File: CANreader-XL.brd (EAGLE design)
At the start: 61 x 66.5 mm, 77 parts, among them IC2 TJA1055T, IC3 BD9G101G, IC4 LM1117IMPX-3.3, IC5 STM32F107VBT, Q1 16MHz, SW1 SLEEP, SW2 TERM, U1 HC_05, U2 MCP2551, X1 MINI-USB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

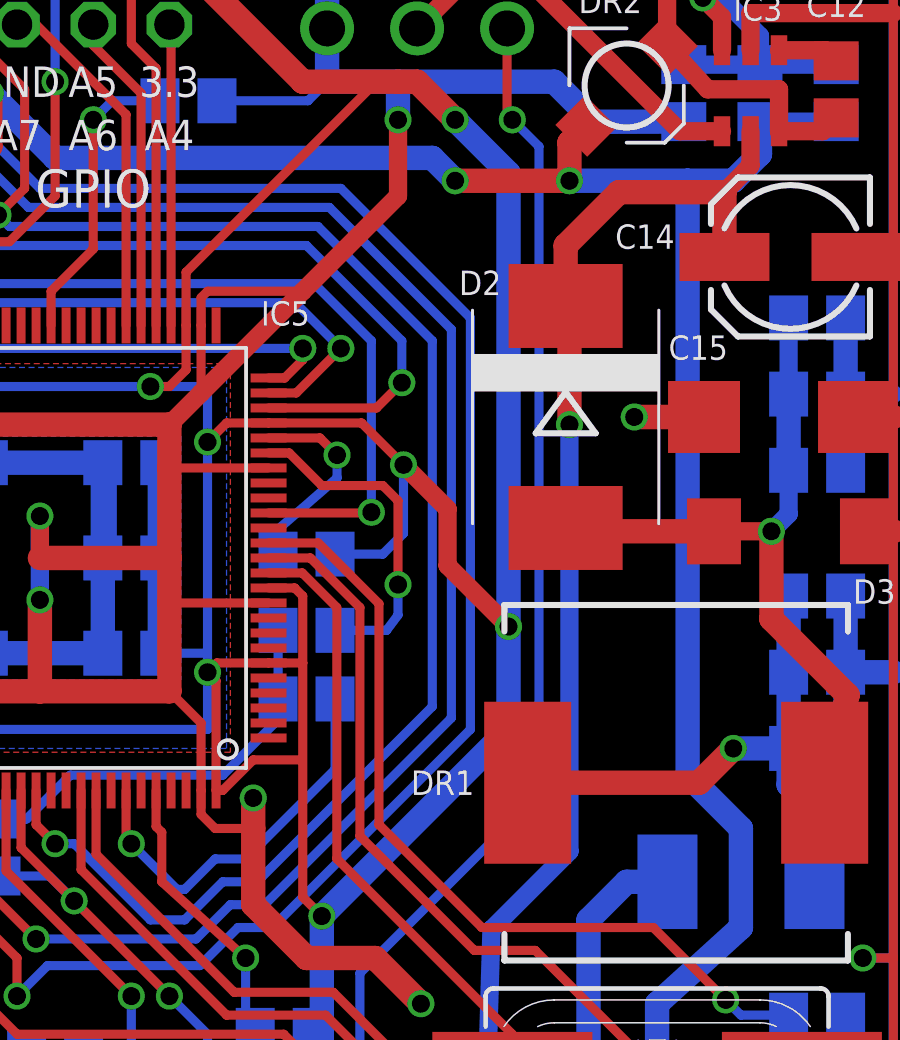
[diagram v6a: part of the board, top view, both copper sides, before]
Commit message: Move D2
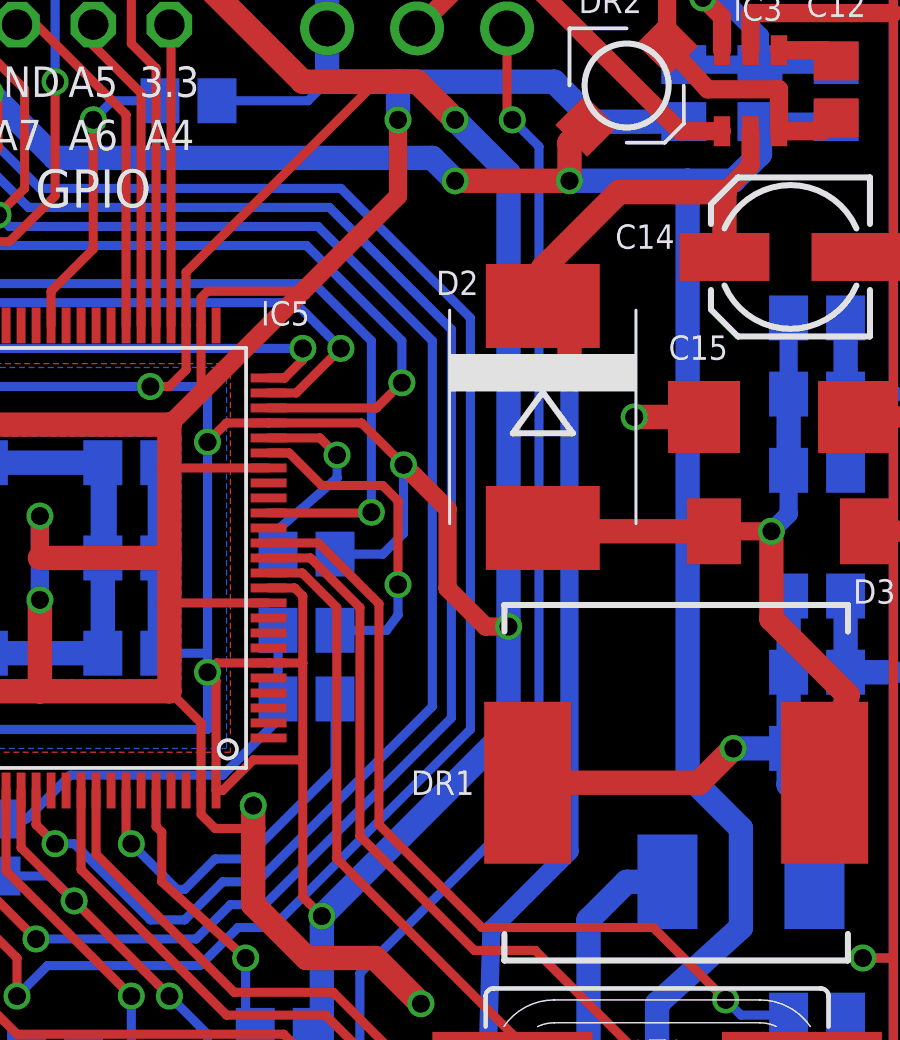
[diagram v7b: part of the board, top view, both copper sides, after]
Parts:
- moved D2 0.76 mm to (48.0, 44.7)
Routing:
- net BAT: track 43.1 -> 44.1 mm
- net BAT1: track 26.4 -> 27.2 mm
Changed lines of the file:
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@@
 <layer number="19" name="Unrouted" color="6" fill="1" visible="yes" active="yes"/>
 <layer number="20" name="Dimension" color="15" fill="1" visible="yes" active="yes"/>
-<layer number="21" name="tPlace" color="7" fill="1" visible="no" active="yes"/>
-<layer number="22" name="bPlace" color="7" fill="1" visible="yes" active="yes"/>
-<layer number="23" name="tOrigins" color="15" fill="1" visible="no" active="yes"/>
-<layer number="24" name="bOrigins" color="15" fill="1" visible="yes" active="yes"/>
-<layer number="25" name="tNames" color="7" fill="1" visible="no" active="yes"/>
-<layer number="26" name="bNames" color="7" fill="1" visible="yes" active="yes"/>
+<layer number="21" name="tPlace" color="7" fill="1" visible="yes" active="yes"/>
+<layer number="22" name="bPlace" color="7" fill="1" visible="no" active="yes"/>
+<layer number="23" name="tOrigins" color="15" fill="1" visible="yes" active="yes"/>
+<layer number="24" name="bOrigins" color="15" fill="1" visible="no" active="yes"/>
+<layer number="25" name="tNames" color="7" fill="1" visible="yes" active="yes"/>
+<layer number="26" name="bNames" color="7" fill="1" visible="no" active="yes"/>
 <layer number="27" name="tValues" color="7" fill="1" visible="no" active="yes"/>
 <layer number="28" name="bValues" color="7" fill="1" visible="no" active="yes"/>
@@
 <layer number="49" name="Reference" color="7" fill="1" visible="no" active="yes"/>
 <layer number="51" name="tDocu" color="7" fill="1" visible="no" active="yes"/>
-<layer number="52" name="bDocu" color="7" fill="1" visible="yes" active="yes"/>
+<layer number="52" name="bDocu" color="7" fill="1" visible="no" active="yes"/>
 <layer number="53" name="tGND_GNDA" color="7" fill="9" visible="no" active="no"/>
 <layer number="54" name="bGND_GNDA" color="1" fill="9" visible="no" active="no"/>
@@
 <attribute name="VALUE" x="53.975" y="42.164" size="1.016" layer="27"/>
 </element>
-<element name="D2" library="diode" package="SMC" value="3A/50V" x="48.768" y="44.704" smashed="yes" rot="R270">
-<attribute name="NAME" x="45.212" y="48.768" size="0.8128" layer="25"/>
-<attribute name="VALUE" x="44.139" y="48.163" size="1.27" layer="27" rot="R270"/>
+<element name="D2" library="diode" package="SMC" value="3A/50V" x="48.006" y="44.704" smashed="yes" rot="R270">
+<attribute name="NAME" x="44.45" y="48.768" size="0.8128" layer="25"/>
+<attribute name="VALUE" x="43.377" y="48.163" size="1.27" layer="27" rot="R270"/>
 </element>
 </elements>
@@
 <wire x1="40.132" y1="26.67" x2="38.354" y2="28.448" width="0.8128" layer="1"/>
 <wire x1="38.354" y1="28.448" x2="38.354" y2="30.988" width="0.8128" layer="1"/>
-<via x="38.354" y="32.004" extent="1-16" drill="0.6"/>
-<wire x1="38.354" y1="30.988" x2="38.354" y2="32.004" width="0.8128" layer="1"/>
+<via x="38.354" y="31.75" extent="1-16" drill="0.6"/>
+<wire x1="38.354" y1="30.988" x2="38.354" y2="31.75" width="0.8128" layer="1"/>
 <wire x1="36.615" y1="32.255" x2="36.615" y2="31.457" width="0.3048" layer="1"/>
 <wire x1="36.615" y1="31.457" x2="37.084" y2="30.988" width="0.3048" layer="1"/>
@@
 <wire x1="6.03" y1="42.926" x2="11.43" y2="42.926" width="0.6096" layer="16"/>
 <via x="46.863" y="37.719" extent="1-16" drill="0.6"/>
-<wire x1="44.831" y1="41.639" x2="44.831" y2="39.751" width="0.6096" layer="1"/>
-<wire x1="44.831" y1="39.751" x2="46.863" y2="37.719" width="0.6096" layer="1"/>
+<wire x1="44.831" y1="41.639" x2="44.831" y2="38.989" width="0.6096" layer="1"/>
 <wire x1="25.908" y1="24.892" x2="25.908" y2="20.32" width="0.8128" layer="16"/>
 <wire x1="20.828" y1="20.32" x2="20.828" y2="23.876" width="0.8128" layer="1"/>
@@
 <wire x1="38.354" y1="33.274" x2="39.878" y2="33.274" width="0.3048" layer="1"/>
 <wire x1="40.64" y1="28.067" x2="40.005" y2="28.702" width="0.3048" layer="1"/>
+<wire x1="46.863" y1="37.719" x2="46.101" y2="37.719" width="0.6096" layer="1"/>
+<wire x1="46.101" y1="37.719" x2="44.831" y2="38.989" width="0.6096" layer="1"/>
 </signal>
 <signal name="CAN1_RX">
@@
 <wire x1="53.711" y1="40.894" x2="48.768" y2="40.894" width="0.8128" layer="1"/>
 <wire x1="48.768" y1="40.894" x2="48.785" y2="41.021" width="0.8128" layer="1"/>
-<wire x1="48.785" y1="41.021" x2="48.768" y2="41.004" width="0.8128" layer="1"/>
+<wire x1="48.785" y1="41.021" x2="48.006" y2="41.004" width="0.8128" layer="1"/>
 <wire x1="56.2" y1="45.466" x2="56.2" y2="41.468" width="0.6096" layer="16"/>
 <wire x1="56.2" y1="41.468" x2="55.626" y2="40.894" width="0.6096" layer="16"/>
@@
 <signal name="BAT">
 <contactref element="R4" pad="2"/>
-<via x="48.895" y="44.45" extent="1-16" drill="0.6"/>
-<wire x1="48.895" y1="44.45" x2="48.895" y2="30.226" width="0.6096" layer="16"/>
+<via x="48.895" y="45.974" extent="1-16" drill="0.6"/>
+<wire x1="48.895" y1="45.974" x2="48.895" y2="30.226" width="0.6096" layer="16"/>
 <wire x1="48.895" y1="30.226" x2="46.294" y2="27.625" width="0.6096" layer="16"/>
 <wire x1="46.294" y1="27.625" x2="46.04" y2="19.05" width="0.6096" layer="16"/>
@@
 <wire x1="54.93" y1="53.086" x2="54.061" y2="52.197" width="0.6096" layer="1"/>
 <wire x1="54.061" y1="52.197" x2="50.546" y2="52.197" width="0.8128" layer="1"/>
-<wire x1="50.546" y1="52.197" x2="48.768" y2="50.419" width="0.8128" layer="1"/>
+<wire x1="50.546" y1="52.197" x2="48.006" y2="49.657" width="0.8128" layer="1"/>
 <contactref element="C14" pad="+"/>
 <contactref element="D2" pad="C"/>
-<wire x1="48.768" y1="50.419" x2="48.768" y2="48.404" width="0.8128" layer="1"/>
-<wire x1="48.895" y1="44.45" x2="48.895" y2="48.277" width="0.8128" layer="1"/>
-<wire x1="48.895" y1="48.277" x2="48.768" y2="48.404" width="0.6096" layer="1"/>
+<wire x1="48.006" y1="49.657" x2="48.006" y2="48.404" width="0.8128" layer="1"/>
+<wire x1="48.895" y1="45.974" x2="48.895" y2="48.277" width="0.8128" layer="1"/>
+<wire x1="48.895" y1="48.277" x2="48.006" y2="48.404" width="0.6096" layer="1"/>
 <wire x1="54.061" y1="50.038" x2="54.061" y2="52.197" width="0.8128" layer="1"/>
 </signal>

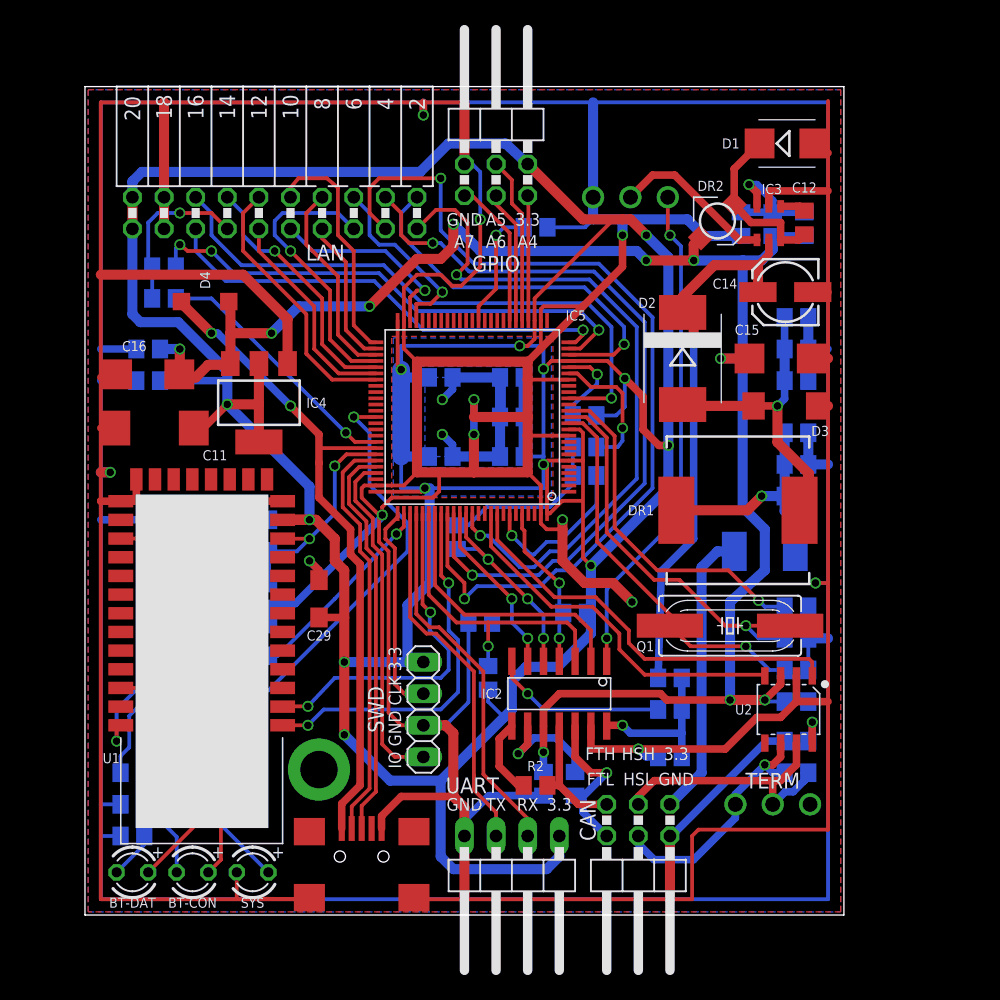
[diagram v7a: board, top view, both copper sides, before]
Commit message: Connectors silk
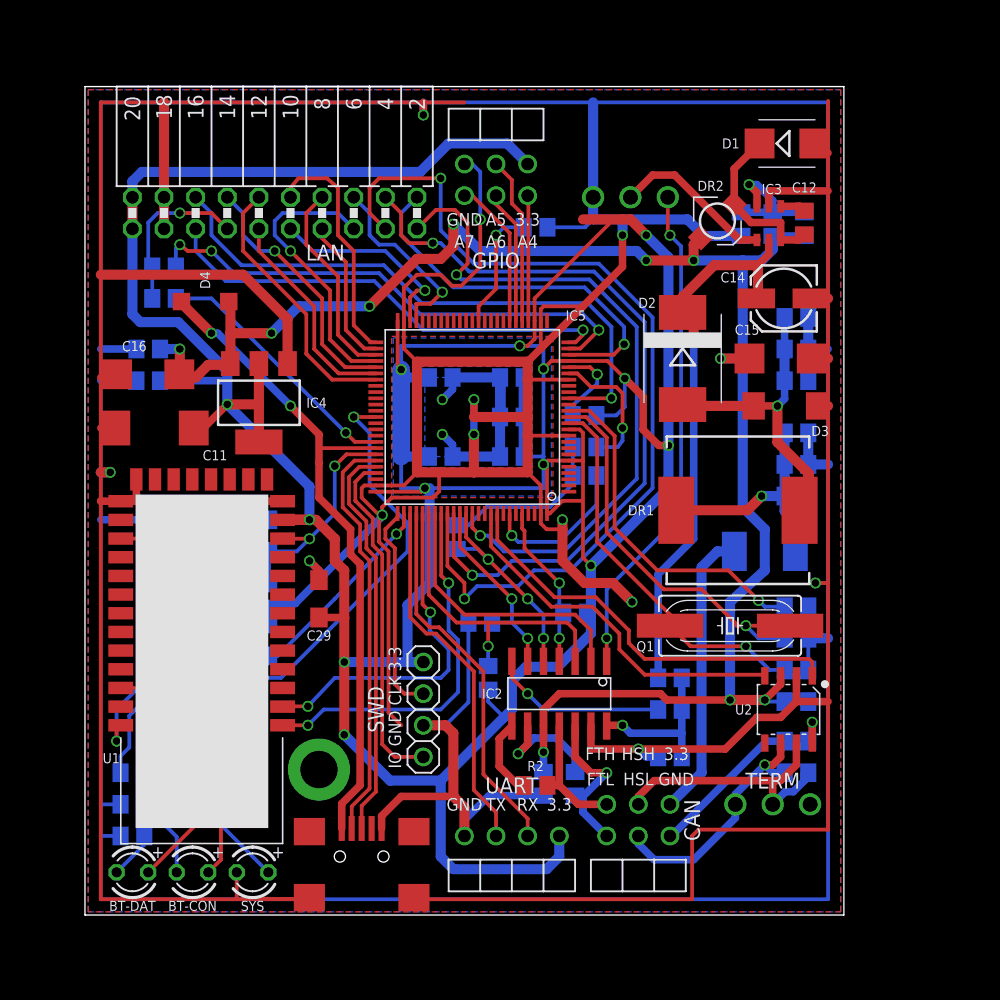
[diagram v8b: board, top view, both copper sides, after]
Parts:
- X2: device pinhead:1X04 -> STM32_CAN-USB:1X04
- X3, X5: device pinhead:2X03/90 -> STM32_CAN-USB:2X03/90
- X4: device pinhead:1X04/90 -> STM32_CAN-USB:1X04/90
- moved C14 0.52 mm to (56.1, 49.5)
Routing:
- net GND: track 898.9 -> 878.3 mm
- net +3V3: track 359.2 -> 352.8 mm
- net PD7: track 56.7 -> 55.6 mm
- net N$3: track 13.3 -> 12.4 mm
- net BAT: track 44.1 -> 44.8 mm
- net N$2: track 33.5 -> 32.8 mm
